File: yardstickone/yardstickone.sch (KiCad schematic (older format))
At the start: 74 parts, among them J1 USB-DEVICE, P1 CONN_02X07, P2 SMA-EDGE, P3 RESET_N, P4 DD, P5 DC, P6 3V3, P7 GND, Q1 MOSFET_P, T1 BALUN, U1 CC1111, U2 AP7313, U3 DMC2400, U4 RX_AMP, U5 SKY13385, U6 SKY13385, U7 TX_AMP, U8 DMC2400, U9 LPF, X1 CRYSTAL

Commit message: YS1 hardware: Update for "modern" KiCAD.
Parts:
- C1, C10, C11, C12, C13, C14, C15, C16, C17, C18, C19, C2, C20, C21, C22, C23, C24, C25, C26, C27, C28, C29, C3, C30, C4, C5, C6, C7, C8, C9: symbol C -> Device:C
- D1, D2, D3: symbol LED -> Device:LED
- D4: symbol GSG-DIODE-TVS-BI -> cc1111:GSG-DIODE-TVS-BI
- FB1: symbol FILTER -> Device:Ferrite_Bead
- J1: symbol USB-DEVICE -> cc1111:USB-DEVICE
- L1, L2: symbol INDUCTOR -> Device:L
- P1: symbol CONN_02X07 -> Connector_Generic:Conn_02x07_Odd_Even
- P2: symbol RF-CONN -> cc1111:RF-CONN
- P3, P4, P5, P6, P7: symbol CONN_1 -> Connector:TestPoint
- Q1: footprint sot23:SOT23-3GDS -> Package_TO_SOT_SMD:SOT-23; symbol MOSFET_P -> Transistor_FET:BSS84
- R1, R10, R11, R12, R14, R15, R17, R2, R3, R4, R5, R6, R8, R9: symbol R -> Device:R
- R13, R16, R7: symbol R-SHORTED -> cc1111:R-SHORTED
- T1: symbol BALUN-B0310J50100AHF -> cc1111:BALUN-B0310J50100AHF
- U1: symbol CC1111 -> cc1111:CC1111
- U2: symbol AP7313 -> cc1111:AP7313
- U3, U8: symbol DMC2400 -> cc1111:DMC2400
- U4: symbol BGA420 -> cc1111:BGA420
- U5, U6: symbol SKY13385 -> cc1111:SKY13385
- U7: symbol SPF5043Z -> cc1111:SPF5043Z
- U9: symbol 0915LP15B026 -> cc1111:0915LP15B026
- X1: symbol CRYSTAL -> usb2412:CRYSTAL
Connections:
- net ANT_BIAS_EN_N: now also Q1.1 (G); no longer Q1.G
- net at L2.1: now also Q1.3 (D); no longer Q1.D
- net 3V3 renamed +3V3
- net +3V3: now also Q1.2 (S); no longer Q1.S

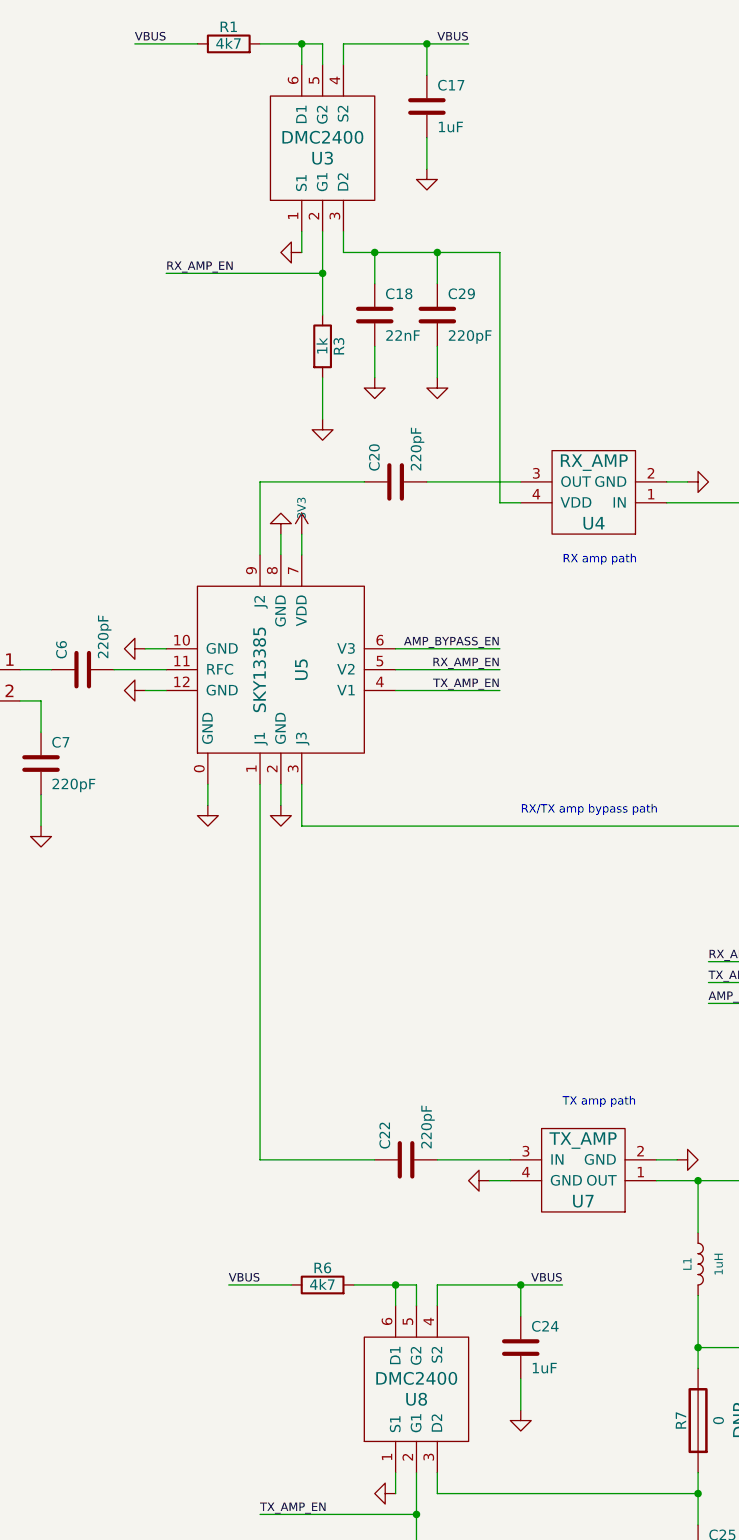
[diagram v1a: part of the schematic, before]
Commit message: YS1 hardware: Replace DMC2400UV with SSM6L36FE,LM.
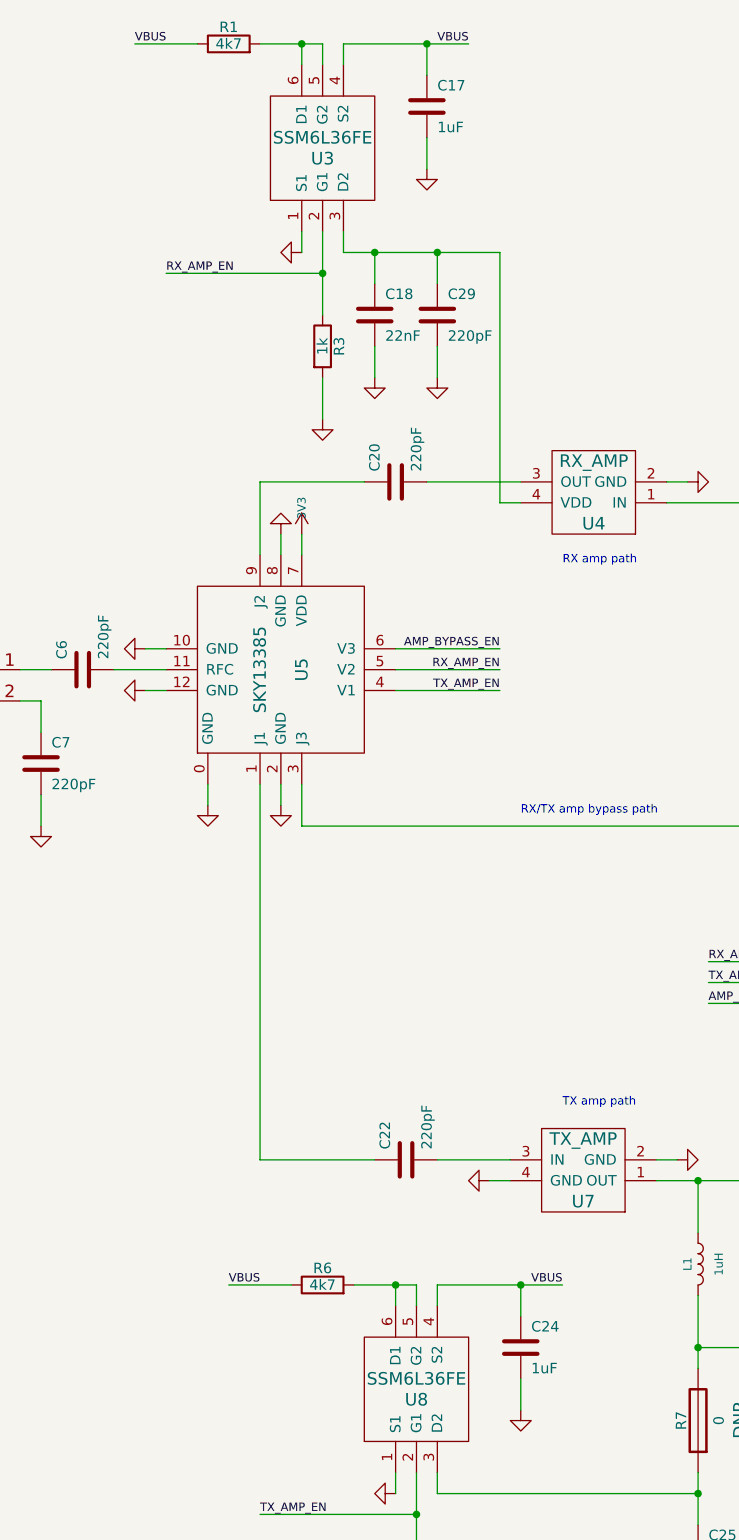
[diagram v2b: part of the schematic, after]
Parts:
- U3, U8: value DMC2400 -> SSM6L36FE; Part Number DMC2400UV-7 -> SSM6L36FE,LM
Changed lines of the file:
@@
 P 10400 7400
 F 0 "U8" V 10350 7400 60  0000 C CNN
-F 1 "DMC2400" V 10450 7400 60  0000 C CNN
+F 1 "SSM6L36FE" V 10450 7400 60  0000 C CNN
 F 2 "cc1111-legacy:GSG-SOT563" H 10400 7400 60  0001 C CNN
 F 3 "" H 10400 7400 60  0001 C CNN
 F 4 "Diodes Inc" H 10400 7400 60  0001 C CNN "Manufacturer"
-F 5 "DMC2400UV-7" H 10400 7400 60  0001 C CNN "Part Number"
+F 5 "SSM6L36FE,LM" H 10400 7400 60  0001 C CNN "Part Number"
 F 6 "MOSFET N P CH 20V SOT563" H 10400 7400 60  0001 C CNN "Description"
 	1    10400 7400
@@
 P 9950 1450
 F 0 "U3" V 9900 1450 60  0000 C CNN
-F 1 "DMC2400" V 10000 1450 60  0000 C CNN
+F 1 "SSM6L36FE" V 10000 1450 60  0000 C CNN
 F 2 "cc1111-legacy:GSG-SOT563" H 9950 1450 60  0001 C CNN
 F 3 "" H 9950 1450 60  0001 C CNN
 F 4 "Diodes Inc" H 9950 1450 60  0001 C CNN "Manufacturer"
-F 5 "DMC2400UV-7" H 9950 1450 60  0001 C CNN "Part Number"
+F 5 "SSM6L36FE,LM" H 9950 1450 60  0001 C CNN "Part Number"
 F 6 "MOSFET N P CH 20V SOT563" H 9950 1450 60  0001 C CNN "Description"
 	1    9950 1450

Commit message: YS1 hardware: More KiCAD 5 cleanup
Update LED symbol orientation
Update LED footprint and footprint orientation
Correct U3 & U8 Manufacturer
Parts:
- D1, D2, D3: footprint cc1111-legacy:GSG-0603D -> Diode_SMD:D_0603_1608Metric
- Q1: Manufacturer Fairchield -> onsemi
- U3, U8: Manufacturer Diodes Inc -> Toshiba
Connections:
- net GND: now also D1.1 (K), D2.1 (K), D3.1 (K); no longer D1.2 (A), D2.2 (A), D3.2 (A)
- net at R5.1: now also D1.2 (A); no longer D1.1 (K)
- net at R11.1: now also D2.2 (A); no longer D2.1 (K)
- net at R12.1: now also D3.2 (A); no longer D3.1 (K)
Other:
- moved on the sheet: D1, D2, D3
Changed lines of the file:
@@
 F 2 "cc1111-legacy:GSG-SOT563" H 10400 7400 60  0001 C CNN
 F 3 "" H 10400 7400 60  0001 C CNN
-F 4 "Diodes Inc" H 10400 7400 60  0001 C CNN "Manufacturer"
+F 4 "Toshiba" H 10400 7400 60  0001 C CNN "Manufacturer"
 F 5 "SSM6L36FE,LM" H 10400 7400 60  0001 C CNN "Part Number"
 F 6 "MOSFET N P CH 20V SOT563" H 10400 7400 60  0001 C CNN "Description"
@@
 F 2 "cc1111-legacy:GSG-SOT563" H 9950 1450 60  0001 C CNN
 F 3 "" H 9950 1450 60  0001 C CNN
-F 4 "Diodes Inc" H 9950 1450 60  0001 C CNN "Manufacturer"
+F 4 "Toshiba" H 9950 1450 60  0001 C CNN "Manufacturer"
 F 5 "SSM6L36FE,LM" H 9950 1450 60  0001 C CNN "Part Number"
 F 6 "MOSFET N P CH 20V SOT563" H 9950 1450 60  0001 C CNN "Description"
@@
 F 0 "D3" H 2200 4000 50  0000 C CNN
 F 1 "LED3" H 2200 3800 50  0000 C CNN
-F 2 "cc1111-legacy:GSG-0603D" H 2200 3900 60  0001 C CNN
+F 2 "Diode_SMD:D_0603_1608Metric" H 2200 3900 60  0001 C CNN
 F 3 "" H 2200 3900 60  0001 C CNN
 F 4 "Kingbright" H 2200 3900 60  0001 C CNN "Manufacturer"
@@
 F 6 "LED 1.6X0.8MM 588NM YLW CLR SMD" H 2200 3900 60  0001 C CNN "Description"
 	1    2200 3900
-	0    1    1    0
+	0    -1   -1   0
 $EndComp
 $Comp
@@
 F 0 "D2" H 1700 4000 50  0000 C CNN
 F 1 "LED2" H 1700 3800 50  0000 C CNN
-F 2 "cc1111-legacy:GSG-0603D" H 1700 3900 60  0001 C CNN
+F 2 "Diode_SMD:D_0603_1608Metric" H 1700 3900 60  0001 C CNN
 F 3 "" H 1700 3900 60  0001 C CNN
 F 4 "Kingbright" H 1700 3900 60  0001 C CNN "Manufacturer"
@@
 F 6 "LED 1.6X0.8MM 625NM RED CLR SMD" H 1700 3900 60  0001 C CNN "Description"
 	1    1700 3900
-	0    1    1    0
+	0    -1   -1   0
 $EndComp
 $Comp
@@
 F 0 "D1" H 1200 4000 50  0000 C CNN
 F 1 "LED1" H 1200 3800 50  0000 C CNN
-F 2 "cc1111-legacy:GSG-0603D" H 1200 3900 60  0001 C CNN
+F 2 "Diode_SMD:D_0603_1608Metric" H 1200 3900 60  0001 C CNN
 F 3 "" H 1200 3900 60  0001 C CNN
 F 4 "Kingbright" H 1200 3900 60  0001 C CNN "Manufacturer"
@@
 F 6 "LED 1.6X0.8MM 568NM GRN CLR SMD" H 1200 3900 60  0001 C CNN "Description"
 	1    1200 3900
-	0    1    1    0
+	0    -1   -1   0
 $EndComp
 Text Label 4700 2400 0    40   ~ 0
@@
 $EndComp
 $Comp
-L power:+3V3 #PWR063
-U 1 1 50C67AB4
-P 13250 1600
-F 0 "#PWR063" H 13250 1700 40  0001 C CNN
-F 1 "3V3" V 13250 1725 40  0000 C CNN
-F 2 "" H 13250 1600 60  0001 C CNN
-F 3 "" H 13250 1600 60  0001 C CNN
-	1    13250 1600
-	1    0    0    -1
-$EndComp
-$Comp
 L power:+3V3 #PWR064
 U 1 1 50C67ABA
@@
 F 2 "Package_TO_SOT_SMD:SOT-23" H 15300 4150 60  0001 C CNN
 F 3 "" H 15300 4150 60  0000 C CNN
-F 4 "Fairchield" H 15300 4150 60  0001 C CNN "Manufacturer"
+F 4 "onsemi" H 15300 4150 60  0001 C CNN "Manufacturer"
 F 5 "BSS84" H 15300 4150 60  0001 C CNN "Part Number"
 F 6 "MOSFET P-CH 50V 130MA SOT-23" H 15300 4150 60  0001 C CNN "Description"
@@
 	2750 6950 3350 6950
 Connection ~ 2750 6950
+$Comp
+L power:+3V3 #PWR063
+U 1 1 50C67AB4
+P 13250 1600
+F 0 "#PWR063" H 13250 1700 40  0001 C CNN
+F 1 "3V3" V 13250 1725 40  0000 C CNN
+F 2 "" H 13250 1600 60  0001 C CNN
+F 3 "" H 13250 1600 60  0001 C CNN
+	1    13250 1600
+	1    0    0    -1
+$EndComp
 $EndSCHEMATC
